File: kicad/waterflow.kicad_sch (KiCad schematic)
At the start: 15 parts, among them J1 Terminal, Q1 BC547, Q2 BC547, Q3 AO4447, U1 WeMos_D1_mini

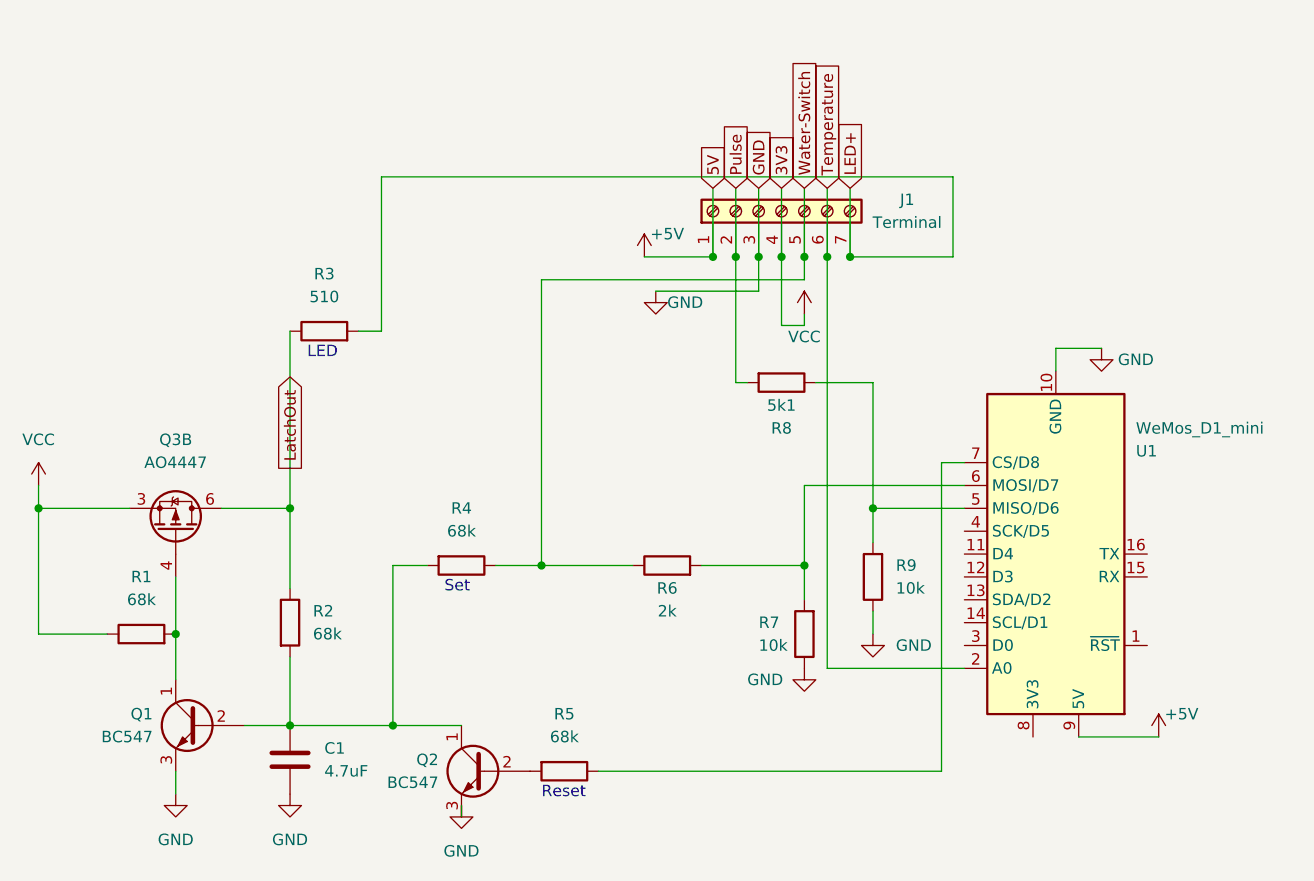
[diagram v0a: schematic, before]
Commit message: fixed: LED+ is now LOUT
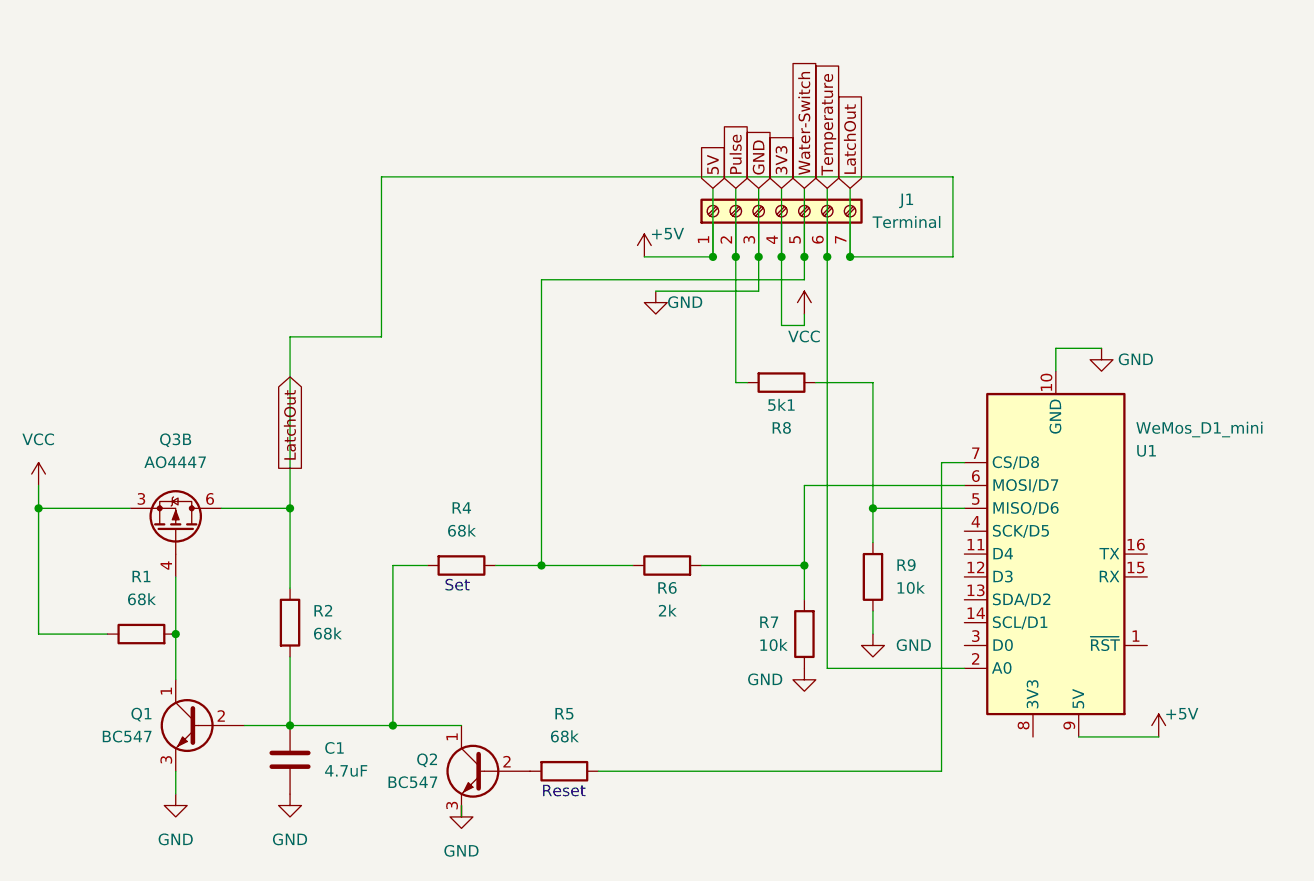
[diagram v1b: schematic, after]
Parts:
- removed R3: 510, Resistor_THT:R_Axial_DIN0207_L6.3mm_D2.5mm_P10.16mm_Horizontal, symbol Device:R
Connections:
- net LED+ is gone; now on net LatchOut: J1.7 (Pin_7)
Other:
- note removed: "LED"
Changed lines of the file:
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@@
+    (stroke (width 0) (type default) (color 0 0 0 0))
+  )
+  (wire (pts (xy 135.89 60.96) (xy 125.73 60.96))
     (stroke (width 0) (type default) (color 0 0 0 0))
   )
@@
     (stroke (width 0) (type default) (color 0 0 0 0))
   )
-  (wire (pts (xy 135.89 43.18) (xy 135.89 60.325))
-    (stroke (width 0) (type default) (color 0 0 0 0))
-  )
   (wire (pts (xy 137.16 86.36) (xy 140.97 86.36))
     (stroke (width 0) (type default) (color 0 0 0 0))
@@
     (stroke (width 0) (type default) (color 0 0 0 0))
   )
-  (wire (pts (xy 125.73 60.325) (xy 125.73 80.01))
+  (wire (pts (xy 125.73 60.96) (xy 125.73 80.01))
     (stroke (width 0) (type default) (color 0 0 0 0))
   )
@@
     (stroke (width 0) (type default) (color 0 0 0 0))
   )
-  (wire (pts (xy 133.35 60.325) (xy 135.89 60.325))
-    (stroke (width 0) (type default) (color 0 0 0 0))
-  )
   (wire (pts (xy 113.03 87.63) (xy 113.03 93.98))
     (stroke (width 0) (type default) (color 0 0 0 0))
@@
     (stroke (width 0) (type default) (color 0 0 0 0))
   )
+  (wire (pts (xy 135.89 43.18) (xy 135.89 60.96))
+    (stroke (width 0) (type default) (color 0 0 0 0))
+  )
   (wire (pts (xy 175.26 44.45) (xy 175.26 52.07))
     (stroke (width 0) (type default) (color 0 0 0 0))
@@
   (wire (pts (xy 144.78 114.3) (xy 144.78 113.03))
     (stroke (width 0) (type default) (color 0 0 0 0))
-  )
-  (text "LED" (at 127.635 63.5 0)
-    (effects (font (size 1.27 1.27)) (justify left bottom))
   )
   (text "Set" (at 142.875 89.535 0)
@@
     )
   )
-  (global_label "LED+" (shape input) (at 187.96 44.45 90) (fields_autoplaced)
+  (global_label "LatchOut" (shape input) (at 187.96 44.45 90) (fields_autoplaced)
     (effects (font (size 1.27 1.27)) (justify left))
-    (property "Intersheet References" "${INTERSHEET_REFS}" (id 0) (at 187.8806 37.0174 90)
+    (property "Intersheet References" "${INTERSHEET_REFS}" (id 0) (at 187.8806 33.6912 90)
       (effects (font (size 1.27 1.27)) (justify left) hide)
     )
@@
       (effects (font (size 1.27 1.27)) (justify left) hide)
     )
-    (pin "1")
-    (pin "2")
-    (pin "7")
-    (pin "8")
     (pin "3")
     (pin "4")
@@
     (pin "1")
   )
-  (symbol (lib_id "Device:R") (at 129.54 60.325 90) (unit 1)
-    (in_bom yes) (on_board yes) (fields_autoplaced)
-    (property "Reference" "R3" (id 0) (at 129.54 53.975 90))
-    (property "Value" "510" (id 1) (at 129.54 56.515 90))
-    (property "Footprint" "Resistor_THT:R_Axial_DIN0207_L6.3mm_D2.5mm_P10.16mm_Horizontal" (id 2) (at 129.54 62.103 90)
-      (effects (font (size 1.27 1.27)) hide)
-    )
-    (property "Datasheet" "~" (id 3) (at 129.54 60.325 0)
-      (effects (font (size 1.27 1.27)) hide)
-    )
-    (pin "1")
-    (pin "2")
-  )
   (sheet_instances
     (path "/" (page "1"))
@@
       (reference "R2") (unit 1) (value "68k") (footprint "Resistor_THT:R_Axial_DIN0207_L6.3mm_D2.5mm_P10.16mm_Horizontal")
     )
-    (path "/ff095e62-5dc7-4d7b-8c87-90235aac152c"
-      (reference "R3") (unit 1) (value "510") (footprint "Resistor_THT:R_Axial_DIN0207_L6.3mm_D2.5mm_P10.16mm_Horizontal")
-    )
     (path "/974ed2f8-0c8f-4711-b9d3-e8bda781e193"

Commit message: changed: footprint for BC547 (make soldering easier)
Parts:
- Q1, Q2: footprint Package_TO_SOT_THT:TO-92_Inline -> Package_TO_SOT_THT:TO-92_HandSolder
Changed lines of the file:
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@@
       (effects (font (size 1.27 1.27)) (justify left) hide)
     )
+    (pin "1")
+    (pin "2")
+    (pin "7")
+    (pin "8")
     (pin "3")
     (pin "4")
@@
       (effects (font (size 1.27 1.27)) (justify left))
     )
-    (property "Footprint" "Package_TO_SOT_THT:TO-92_Inline" (id 2) (at 142.24 111.125 0)
+    (property "Footprint" "Package_TO_SOT_THT:TO-92_HandSolder" (id 2) (at 142.24 111.125 0)
       (effects (font (size 1.27 1.27) italic) (justify left) hide)
     )
@@
       (effects (font (size 1.27 1.27)) (justify left))
     )
-    (property "Footprint" "Package_TO_SOT_THT:TO-92_Inline" (id 2) (at 110.49 106.045 0)
+    (property "Footprint" "Package_TO_SOT_THT:TO-92_HandSolder" (id 2) (at 110.49 106.045 0)
       (effects (font (size 1.27 1.27) italic) (justify left) hide)
     )
@@
     )
     (path "/cefe2b25-c132-4a9d-862f-6dd88da4c699"
-      (reference "Q1") (unit 1) (value "BC547") (footprint "Package_TO_SOT_THT:TO-92_Inline")
+      (reference "Q1") (unit 1) (value "BC547") (footprint "Package_TO_SOT_THT:TO-92_HandSolder")
     )
     (path "/9bbfad08-d021-4bef-bbf0-7a9a641aafb8"
-      (reference "Q2") (unit 1) (value "BC547") (footprint "Package_TO_SOT_THT:TO-92_Inline")
+      (reference "Q2") (unit 1) (value "BC547") (footprint "Package_TO_SOT_THT:TO-92_HandSolder")
     )
     (path "/09bdf402-54d7-4633-8041-d80b91f019f8"
